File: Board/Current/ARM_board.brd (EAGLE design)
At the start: 101.6 x 81.3 mm, 168 parts, among them IC3 STM32F437VI, IC4 LM358DT, J1 USART/I2C, J10 ANALOG, J11 DGND, J12 DPWR, J13 DIGITAL, J14 SGND, J15 SPWR, J16 SERVO, J2 I2C2/USART3, J3 USART2, J5 SPI, J6 Bluesmirf, J7 SWD, J8 AGND, J9 APWR, Q1 STL4P2UH7, Q2 2STR1230, SW1 SW, U1 LSM330DLC, U10 BAV99, U11 BAV99, U12 USBLC6-2, U13 USBLC6-2, U14 STMPS2171MTR, U15 MC74HC164, U17 ?, U18 ?, U19 ?, U20 ?, U3 NC7SZU04, U4 L6206Q, U5 L6206Q, U6 SI7617, U7 SI7617, U8 SI7617, U9 SI7617, Y2 8MHz

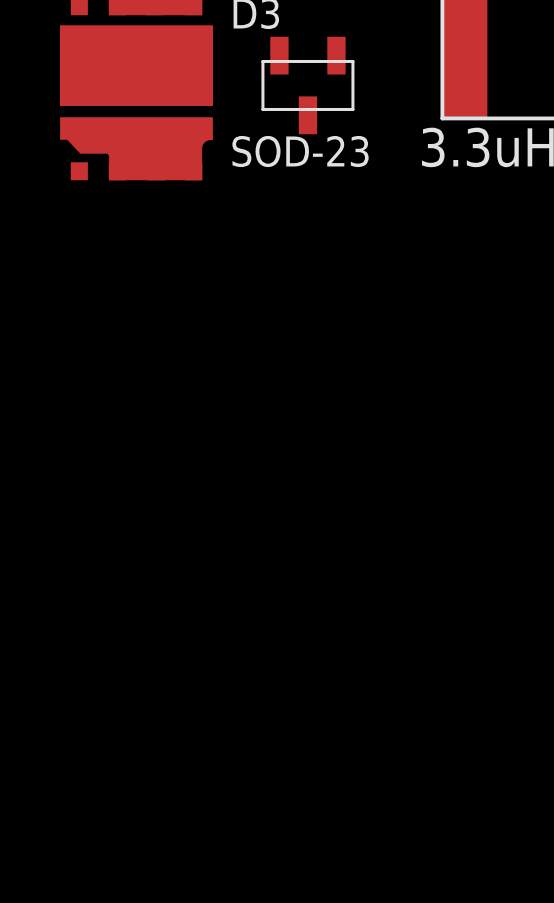
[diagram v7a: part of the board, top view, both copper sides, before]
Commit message: Added more capacitors to entire schematic, including the remaining switching regulator capacitors.
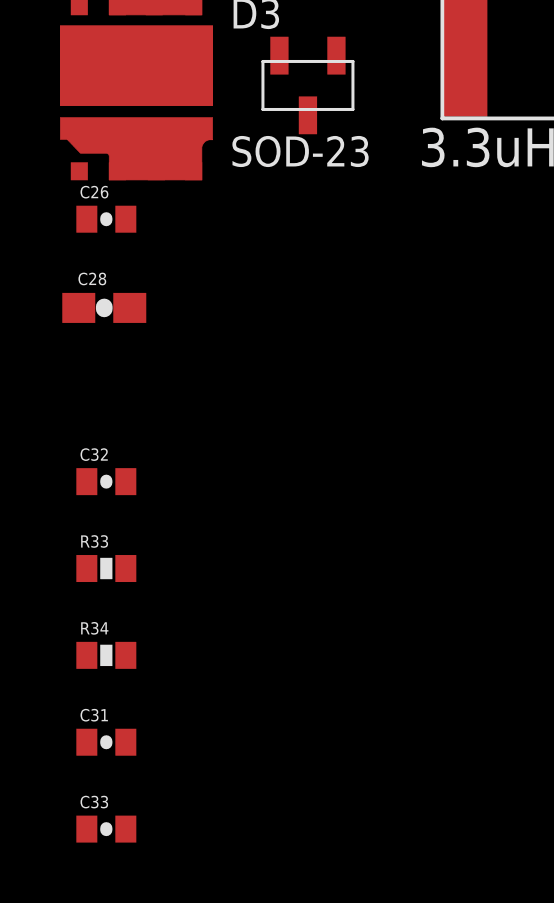
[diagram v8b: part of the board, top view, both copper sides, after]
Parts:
- added C26: 33u, SparkFun:0402-CAP
- added C28: 33u, SparkFun:0603-CAP
- added C31, C32, C33: 0.1u, SparkFun:0402-CAP
- added R33, R34: 1k, SparkFun:0402-RES
- C3, C4: value 15u -> 33u
- C44: value 220u -> 680uF
- C52: value ? -> 680uF
- C6: value 10u -> 33u
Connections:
- net +3V3: now also C31.1, R33.1, R34.1
- net 5V: now also C28.1, C32.1, C33.1
- net GND: now also C26.2, C28.2, C31.2, C32.2, C33.2
- net LCD_CLK: now also R33.2
- net LCD_DATA: now also R34.2
- net VIN: now also C26.1
